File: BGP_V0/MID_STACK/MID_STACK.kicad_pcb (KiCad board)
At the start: 2 copper layers, 30 x 30 mm, 11 parts, among them P1 Conn_01x05, P2 CONN_01X12, U1 OPA170

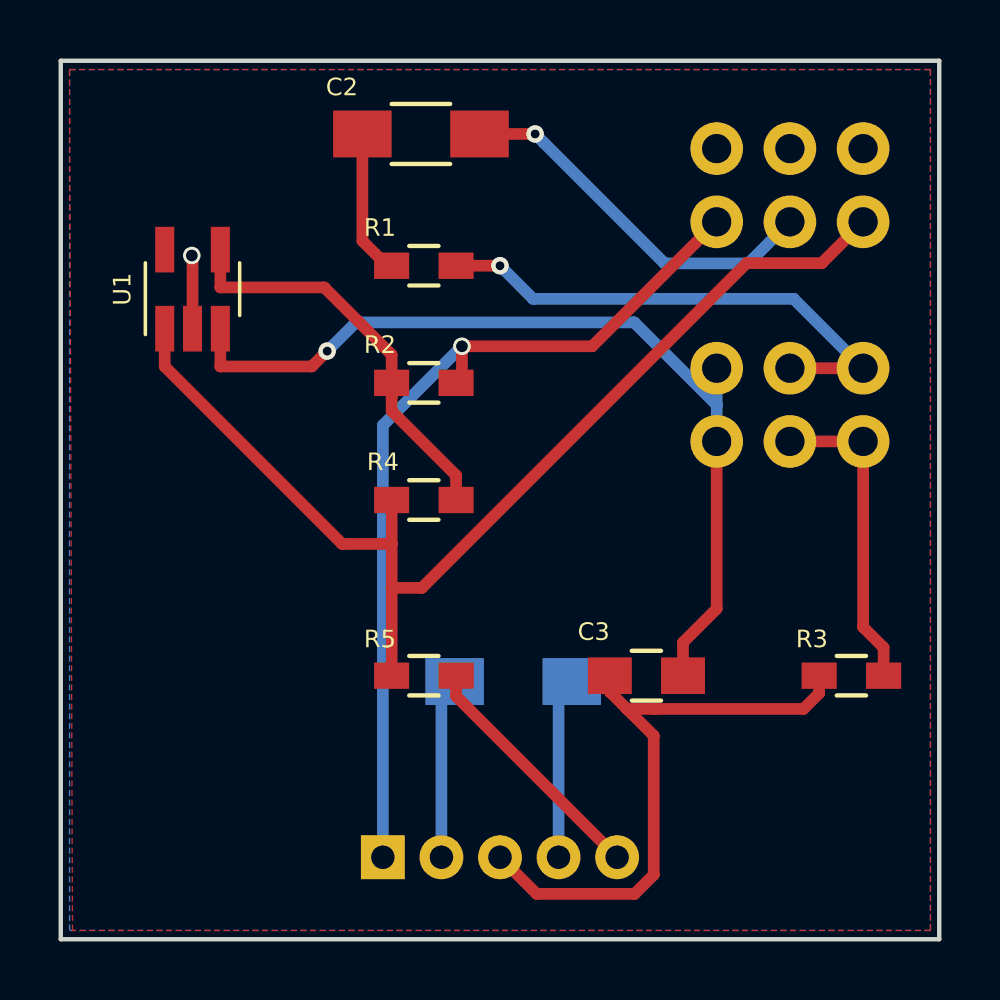
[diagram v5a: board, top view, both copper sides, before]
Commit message: Changed Mid sweep
200 - 2k Hz
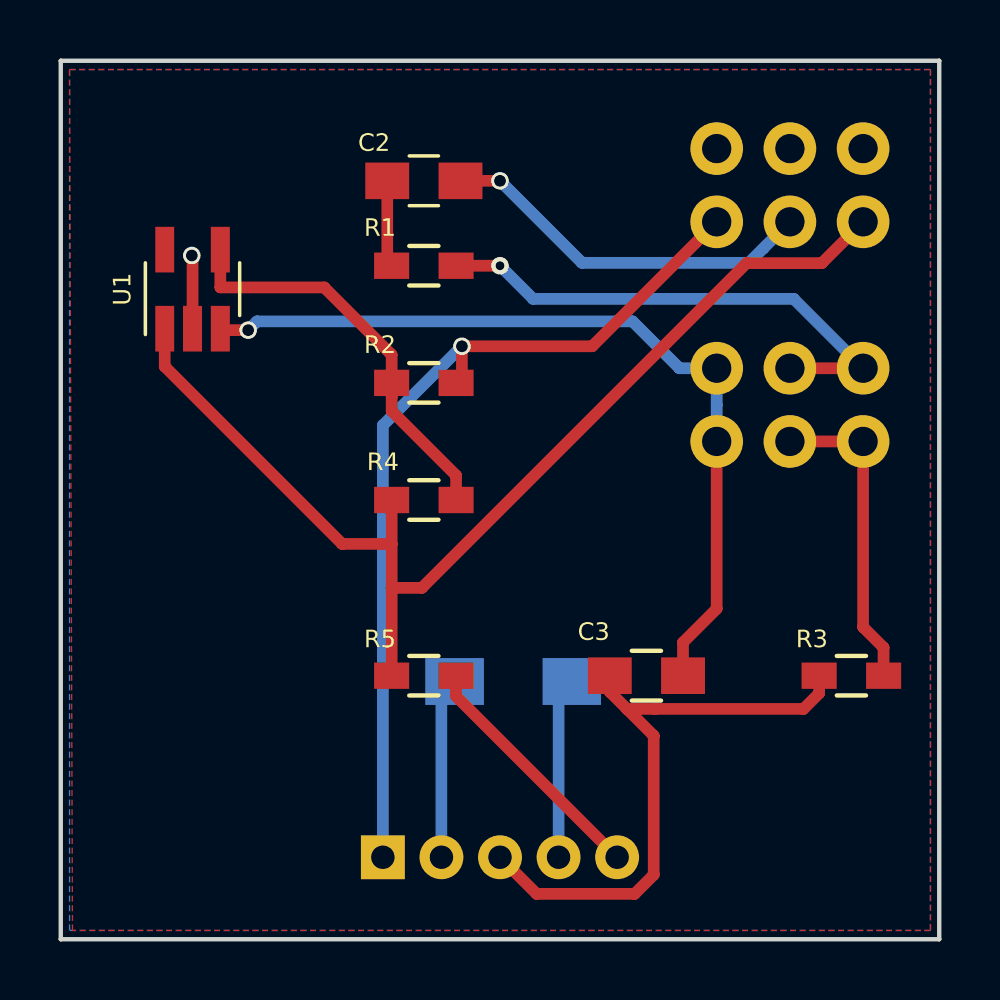
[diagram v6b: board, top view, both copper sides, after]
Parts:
- C2: value 15n -> 10n; footprint Capacitors_SMD:C_1206_HandSoldering -> Capacitors_SMD:C_0805_HandSoldering
- C3: value 6.8n -> 4.7n
- R1, R3: value 6.8k -> 12k
- moved C2 1.60 mm to (156.4, 68.1)
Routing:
- net /F1_1: track 31.0 -> 28.7 mm
- net Net-(C2-Pad2): track 5.00 -> 3.11 mm
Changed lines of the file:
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@@
-(kicad_pcb (version 4) (host pcbnew 4.0.4-1.fc24-product)
+(kicad_pcb (version 4) (host pcbnew 4.0.7)
   (general
     (links 23)
     (no_connects 0)
-    (area 143.924999 63.424999 174.225001 94.979999)
+    (area 143.924999 63.424999 174.225001 94.075001)
     (thickness 1.6)
     (drawings 14)
@@
     (uvia_drill 0.1)
   )
-  (module Capacitors_SMD:C_1206_HandSoldering (layer F.Cu)
-    (at 156.3 66.5 180)
-    (descr "Capacitor SMD 1206, hand soldering")
-    (tags "capacitor 1206")
-    (attr smd)
-    (fp_text reference C2 (at 2.7 1.6 180) (layer F.SilkS)
-      (effects (font (size 0.6 0.6) (thickness 0.15)))
-    )
-    (fp_text value 15n (at -2.4 -1.8 180) (layer F.Fab)
-      (effects (font (size 0.6 0.6) (thickness 0.15)))
-    )
-    (fp_line (start -3.3 -1.15) (end 3.3 -1.15) (layer F.CrtYd) (width 0.05))
-    (fp_line (start -3.3 1.15) (end 3.3 1.15) (layer F.CrtYd) (width 0.05))
-    (fp_line (start -3.3 -1.15) (end -3.3 1.15) (layer F.CrtYd) (width 0.05))
-    (fp_line (start 3.3 -1.15) (end 3.3 1.15) (layer F.CrtYd) (width 0.05))
-    (fp_line (start 1 -1.025) (end -1 -1.025) (layer F.SilkS) (width 0.15))
-    (fp_line (start -1 1.025) (end 1 1.025) (layer F.SilkS) (width 0.15))
-    (pad 1 smd rect (at -2 0 180) (size 2 1.6) (layers F.Cu F.Paste F.Mask)
-      (net 7 /VOL2))
-    (pad 2 smd rect (at 2 0 180) (size 2 1.6) (layers F.Cu F.Paste F.Mask)
-      (net 3 "Net-(C2-Pad2)"))
-    (model Capacitors_SMD.3dshapes/C_1206_HandSoldering.wrl
-      (at (xyz 0 0 0))
-      (scale (xyz 1 1 1))
-      (rotate (xyz 0 0 0))
-    )
-  )
   (module Capacitors_SMD:C_0805_HandSoldering (layer F.Cu)
     (at 164 85 180)
@@
       (effects (font (size 0.6 0.6) (thickness 0.15)))
     )
-    (fp_text value 6.8n (at -1.45 -1.5 180) (layer F.Fab)
+    (fp_text value 4.7n (at -1.45 -1.5 180) (layer F.Fab) hide
       (effects (font (size 0.6 0.6) (thickness 0.15)))
     )
@@
       (effects (font (size 0.6 0.6) (thickness 0.15)))
     )
-    (fp_text value 6.8k (at 1.2 1.3) (layer F.Fab)
+    (fp_text value 12k (at 1.2 1.3) (layer F.Fab) hide
       (effects (font (size 0.6 0.6) (thickness 0.15)))
     )
@@
       (effects (font (size 0.6 0.6) (thickness 0.15)))
     )
-    (fp_text value 22k (at -1.3 -1.3 180) (layer F.Fab)
+    (fp_text value 22k (at -1.3 -1.3 180) (layer F.Fab) hide
       (effects (font (size 0.6 0.6) (thickness 0.15)))
     )
@@
       (effects (font (size 0.6 0.6) (thickness 0.15)))
     )
-    (fp_text value 6.8k (at -1.15 -1.5 180) (layer F.Fab)
+    (fp_text value 12k (at -1.15 -1.5 180) (layer F.Fab) hide
       (effects (font (size 0.6 0.6) (thickness 0.15)))
     )
@@
       (effects (font (size 0.6 0.6) (thickness 0.15)))
     )
-    (fp_text value 22k (at -1.3 -1.4 180) (layer F.Fab)
+    (fp_text value 22k (at -1.3 -1.4 180) (layer F.Fab) hide
       (effects (font (size 0.6 0.6) (thickness 0.15)))
     )
@@
       (effects (font (size 0.6 0.6) (thickness 0.15)))
     )
-    (fp_text value 100 (at 1.25 1.25) (layer F.Fab)
+    (fp_text value 100 (at 1.25 1.25) (layer F.Fab) hide
       (effects (font (size 0.6 0.6) (thickness 0.15)))
     )
@@
     )
   )
+  (module Capacitors_SMD:C_0805_HandSoldering (layer F.Cu)
+    (at 156.4 68.1 180)
+    (descr "Capacitor SMD 0805, hand soldering")
+    (tags "capacitor 0805")
+    (attr smd)
+    (fp_text reference C2 (at 1.7 1.3 180) (layer F.SilkS)
+      (effects (font (size 0.6 0.6) (thickness 0.15)))
+    )
+    (fp_text value 10n (at 0 1.75 180) (layer F.Fab) hide
+      (effects (font (size 0.6 0.6) (thickness 0.15)))
+    )
+    (fp_text user %R (at 0 -1.75 180) (layer F.Fab) hide
+      (effects (font (size 0.6 0.6) (thickness 0.15)))
+    )
+    (fp_line (start -1 0.62) (end -1 -0.62) (layer F.Fab) (width 0.1))
+    (fp_line (start 1 0.62) (end -1 0.62) (layer F.Fab) (width 0.1))
+    (fp_line (start 1 -0.62) (end 1 0.62) (layer F.Fab) (width 0.1))
+    (fp_line (start -1 -0.62) (end 1 -0.62) (layer F.Fab) (width 0.1))
+    (fp_line (start 0.5 -0.85) (end -0.5 -0.85) (layer F.SilkS) (width 0.12))
+    (fp_line (start -0.5 0.85) (end 0.5 0.85) (layer F.SilkS) (width 0.12))
+    (fp_line (start -2.25 -0.88) (end 2.25 -0.88) (layer F.CrtYd) (width 0.05))
+    (fp_line (start -2.25 -0.88) (end -2.25 0.87) (layer F.CrtYd) (width 0.05))
+    (fp_line (start 2.25 0.87) (end 2.25 -0.88) (layer F.CrtYd) (width 0.05))
+    (fp_line (start 2.25 0.87) (end -2.25 0.87) (layer F.CrtYd) (width 0.05))
+    (pad 1 smd rect (at -1.25 0 180) (size 1.5 1.25) (layers F.Cu F.Paste F.Mask)
+      (net 7 /VOL2))
+    (pad 2 smd rect (at 1.25 0 180) (size 1.5 1.25) (layers F.Cu F.Paste F.Mask)
+      (net 3 "Net-(C2-Pad2)"))
+    (model Capacitors_SMD.3dshapes/C_0805.wrl
+      (at (xyz 0 0 0))
+      (scale (xyz 1 1 1))
+      (rotate (xyz 0 0 0))
+    )
+  )
   (gr_text O (at 163 88) (layer B.SilkS)
     (effects (font (size 0.6 0.6) (thickness 0.15)) (justify mirror))
@@
   (segment (start 163.335 86.1353) (end 162.75 85.55) (width 0.4) (layer F.Cu) (net 2))
   (segment (start 164.292 86.1353) (end 163.335 86.1353) (width 0.4) (layer F.Cu) (net 2))
+  (segment (start 155.15 68.1) (end 155.15 70.85) (width 0.4) (layer F.Cu) (net 3))
+  (segment (start 155.15 70.85) (end 155.3 71) (width 0.4) (layer F.Cu) (net 3))
   (segment (start 155.15 71) (end 155.3 71) (width 0.4) (layer F.Cu) (net 3))
-  (segment (start 154.3 70.15) (end 155.15 71) (width 0.4) (layer F.Cu) (net 3))
-  (segment (start 154.3 66.5) (end 154.3 70.15) (width 0.4) (layer F.Cu) (net 3))
   (segment (start 155 91.2) (end 155 76.45) (width 0.4) (layer B.Cu) (net 4))
   (via (at 157.7 73.75) (size 0.6) (drill 0.4) (layers F.Cu B.Cu) (net 4))
@@
   (segment (start 148.5 73.15) (end 148.5 70.674974) (width 0.4) (layer F.Cu) (net 6))
   (via (at 148.475026 70.65) (size 0.6) (drill 0.4) (layers F.Cu B.Cu) (net 6))
-  (via (at 160.2 66.5) (size 0.6) (layers F.Cu B.Cu) (net 7))
-  (segment (start 160.5 66.8) (end 160.2 66.5) (width 0.4) (layer B.Cu) (net 7))
-  (segment (start 164.618 70.9176) (end 160.5 66.8) (width 0.4) (layer B.Cu) (net 7))
-  (segment (start 167.482 70.9176) (end 164.618 70.9176) (width 0.4) (layer B.Cu) (net 7))
-  (segment (start 168.9 69.5) (end 167.482 70.9176) (width 0.4) (layer B.Cu) (net 7))
-  (segment (start 158.3 66.5) (end 160.2 66.5) (width 0.4) (layer F.Cu) (net 7))
-  (via (at 153.0978 73.9146) (size 0.6) (layers F.Cu B.Cu) (net 8))
+  (segment (start 159 68.1) (end 161.800001 70.900001) (width 0.4) (layer B.Cu) (net 7))
+  (segment (start 161.800001 70.900001) (end 167.499999 70.900001) (width 0.4) (layer B.Cu) (net 7))
+  (segment (start 167.499999 70.900001) (end 168.000001 70.399999) (width 0.4) (layer B.Cu) (net 7))
+  (segment (start 168.000001 70.399999) (end 168.9 69.5) (width 0.4) (layer B.Cu) (net 7))
+  (segment (start 157.65 68.1) (end 159 68.1) (width 0.4) (layer F.Cu) (net 7))
+  (via (at 159 68.1) (size 0.6) (drill 0.4) (layers F.Cu B.Cu) (net 7))
+  (segment (start 150.4 73.2) (end 149.5 73.2) (width 0.4) (layer F.Cu) (net 8))
+  (segment (start 149.5 73.2) (end 149.45 73.15) (width 0.4) (layer F.Cu) (net 8))
+  (segment (start 163.527208 72.9) (end 150.7 72.9) (width 0.4) (layer B.Cu) (net 8))
+  (segment (start 150.7 72.9) (end 150.4 73.2) (width 0.4) (layer B.Cu) (net 8))
+  (via (at 150.4 73.2) (size 0.6) (drill 0.4) (layers F.Cu B.Cu) (net 8))
+  (segment (start 166.4 74.5) (end 165.127208 74.5) (width 0.4) (layer B.Cu) (net 8))
+  (segment (start 165.127208 74.5) (end 163.527208 72.9) (width 0.4) (layer B.Cu) (net 8))
   (segment (start 166.4 82.7147) (end 166.4 77) (width 0.4) (layer F.Cu) (net 8))
   (segment (start 165.25 83.8647) (end 166.4 82.7147) (width 0.4) (layer F.Cu) (net 8))
@@
   (segment (start 166.4 74.5) (end 166.4 75.75) (width 0.4) (layer B.Cu) (net 8))
   (segment (start 166.4 75.75) (end 166.4 77) (width 0.4) (layer B.Cu) (net 8))
-  (segment (start 154.0786 72.9338) (end 153.0978 73.9146) (width 0.4) (layer B.Cu) (net 8))
-  (segment (start 163.5838 72.9338) (end 154.0786 72.9338) (width 0.4) (layer B.Cu) (net 8))
-  (segment (start 166.4 75.75) (end 163.5838 72.9338) (width 0.4) (layer B.Cu) (net 8))
-  (segment (start 152.5721 74.4403) (end 149.45 74.4403) (width 0.4) (layer F.Cu) (net 8))
-  (segment (start 153.0978 73.9146) (end 152.5721 74.4403) (width 0.4) (layer F.Cu) (net 8))
-  (segment (start 149.45 73.15) (end 149.45 74.4403) (width 0.4) (layer F.Cu) (net 8))
   (segment (start 169.99 70.9104) (end 171.4 69.5) (width 0.4) (layer F.Cu) (net 9))
   (segment (start 167.424 70.9104) (end 169.99 70.9104) (width 0.4) (layer F.Cu) (net 9))

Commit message: Reduced BT MID board sizes.
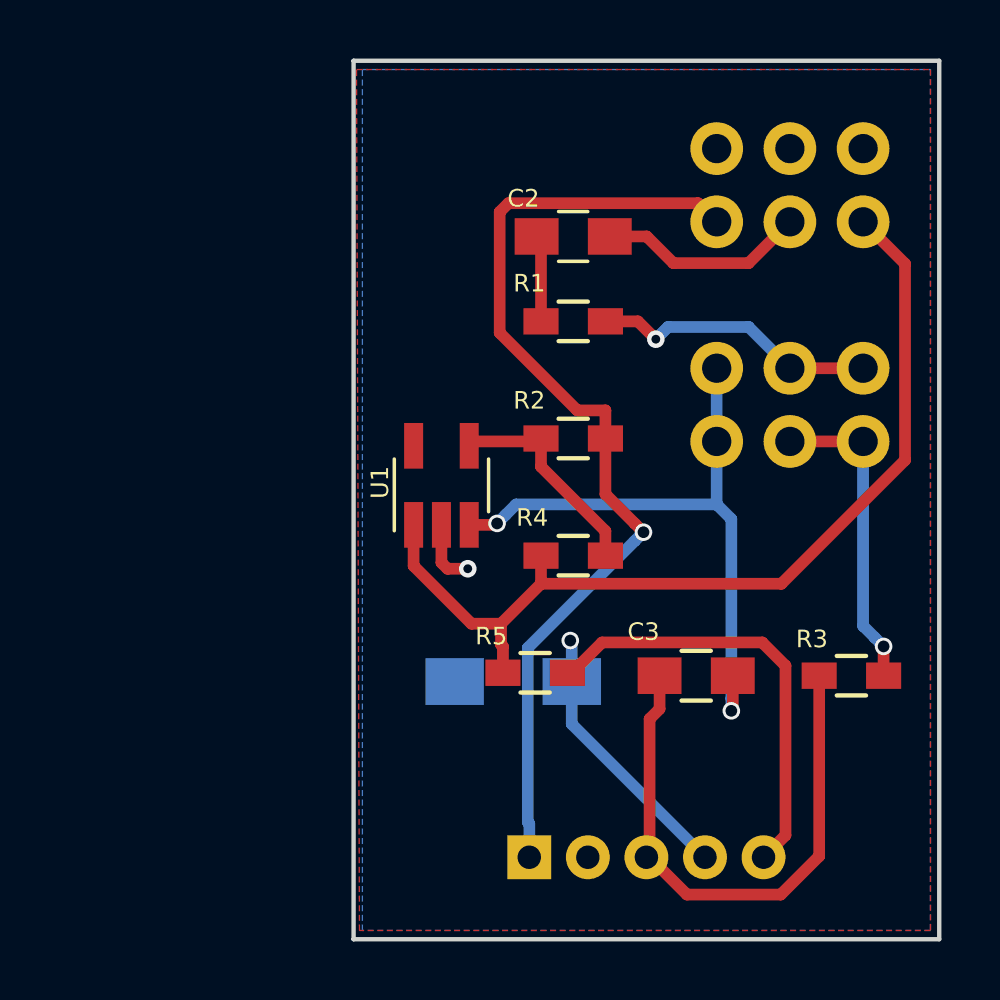
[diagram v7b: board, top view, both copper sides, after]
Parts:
- moved U1 10.8 mm to (157.0, 78.5)
- moved C2 5.44 mm to (161.5, 70.0)
- moved R1 5.44 mm to (161.5, 72.9)
- moved R2 5.44 mm to (161.5, 76.9)
- moved R4 5.44 mm to (161.5, 80.9)
- moved P1 5.00 mm to (160.0, 91.2)
- moved R5 3.80 mm to (160.2, 84.9)
- moved C3 1.70 mm to (165.7, 85.0)
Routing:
- net /F1_2: track 17.8 -> 9.81 mm
- net /F1_1: track 28.7 -> 21.9 mm, vias 1 -> 2
- net /OUT: track 8.48 -> 15.1 mm
- net Net-(R2-Pad2): track 14.0 -> 7.54 mm
- net /V-: track 8.70 -> 2.28 mm
- net /VOL3: track 38.8 -> 32.7 mm
- net /VOL2: track 13.0 -> 7.11 mm, vias 1 -> 0
- net /IN: track 30.4 -> 34.1 mm
- net /V+: track 6.19 -> 9.31 mm, vias 0 -> 1
- net Earth: track 20.8 -> 19.5 mm
- net /F2_2: vias 0 -> 1
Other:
- board size 30 x 30 mm -> 20 x 30 mm
